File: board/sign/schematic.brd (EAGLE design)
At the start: 97.8 x 65.7 mm, 37 parts, among them IC1 STM32F207ZGT, IC3 LM3940, J1 DCJ0202, X2 22-23-2041

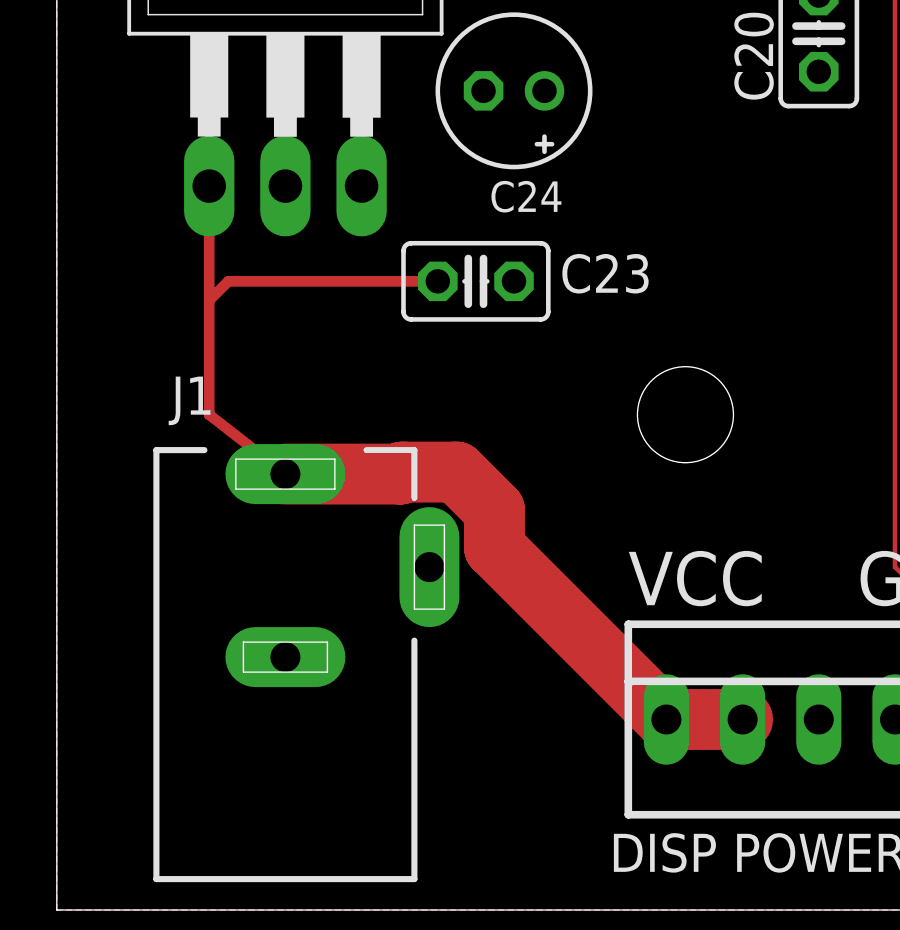
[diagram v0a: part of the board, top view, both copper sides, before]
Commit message: Board trace widths
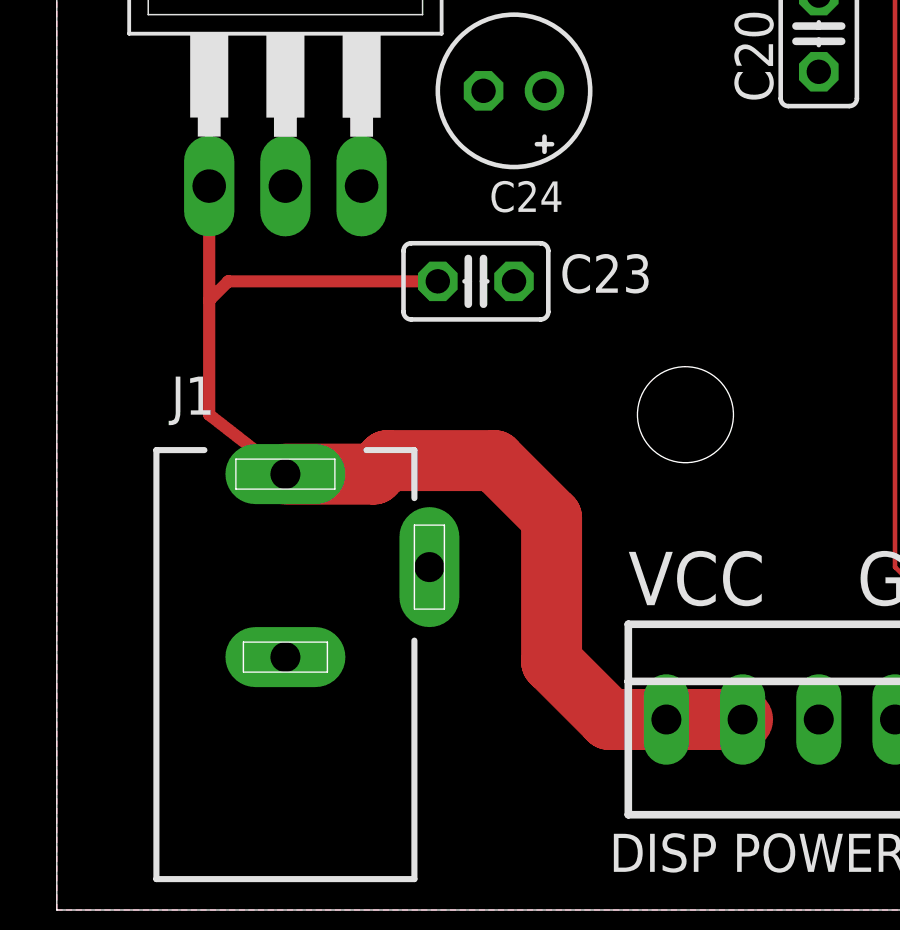
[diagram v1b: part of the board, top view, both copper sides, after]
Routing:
- net +5V: track 38.1 -> 40.5 mm
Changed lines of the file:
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@@
 <drawing>
 <settings>
-<setting alwaysvectorfont="no"/>
+<setting alwaysvectorfont="yes"/>
 <setting verticaltext="up"/>
 </settings>
@@
 <contactref element="IC3" pad="1"/>
 <contactref element="C23" pad="1"/>
-<wire x1="5.08" y1="24.13" x2="5.08" y2="20.32" width="0.3556" layer="1"/>
-<wire x1="5.08" y1="20.32" x2="5.08" y2="16.51" width="0.3556" layer="1"/>
-<wire x1="5.08" y1="16.51" x2="7.62" y2="14.53" width="0.3556" layer="1"/>
-<wire x1="11.52181875" y1="14.5984" x2="13.31818125" y2="14.5984" width="2.032" layer="1"/>
-<wire x1="13.31818125" y1="14.5984" x2="14.5884" y2="13.32818125" width="2.032" layer="1"/>
-<wire x1="14.5884" y1="13.32818125" x2="14.5884" y2="12.0816" width="2.032" layer="1"/>
-<wire x1="14.5884" y1="12.0816" x2="20.32" y2="6.35" width="2.032" layer="1"/>
-<wire x1="7.62" y1="14.53" x2="11.45341875" y2="14.53" width="2.032" layer="1"/>
-<wire x1="11.45341875" y1="14.53" x2="11.52181875" y2="14.5984" width="2.032" layer="1"/>
+<wire x1="5.08" y1="24.13" x2="5.08" y2="20.32" width="0.4064" layer="1"/>
+<wire x1="5.08" y1="20.32" x2="5.08" y2="16.51" width="0.4064" layer="1"/>
+<wire x1="5.08" y1="16.51" x2="7.62" y2="14.53" width="0.4064" layer="1"/>
+<wire x1="11.01381875" y1="14.9794" x2="14.58818125" y2="14.9794" width="2.032" layer="1"/>
+<wire x1="14.58818125" y1="14.9794" x2="16.4934" y2="13.07418125" width="2.032" layer="1"/>
+<wire x1="16.4934" y1="13.07418125" x2="16.4934" y2="8.2716" width="2.032" layer="1"/>
+<wire x1="18.415" y1="6.35" x2="20.32" y2="6.35" width="2.032" layer="1"/>
+<wire x1="18.415" y1="6.35" x2="16.4934" y2="8.2716" width="2.032" layer="1"/>
+<wire x1="7.62" y1="14.53" x2="10.56441875" y2="14.53" width="2.032" layer="1"/>
+<wire x1="10.56441875" y1="14.53" x2="11.01381875" y2="14.9794" width="2.032" layer="1"/>
 <wire x1="22.86" y1="6.35" x2="20.32" y2="6.35" width="2.032" layer="1"/>
-<wire x1="5.08" y1="20.32" x2="5.715" y2="20.955" width="0.3556" layer="1"/>
-<wire x1="5.715" y1="20.955" x2="12.7" y2="20.955" width="0.3556" layer="1"/>
+<wire x1="5.08" y1="20.32" x2="5.715" y2="20.955" width="0.4064" layer="1"/>
+<wire x1="5.715" y1="20.955" x2="12.7" y2="20.955" width="0.4064" layer="1"/>
 </signal>
 <signal name="DEBUG_TX">

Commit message: General trace cleanup
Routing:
- net RESET: track 104.9 -> 105.8 mm
- net B0: track 45.2 -> 45.8 mm
- net DEBUG_TX: track 37.4 -> 36.9 mm
- net D: track 36.0 -> 35.5 mm
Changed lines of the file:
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@@
 <contactref element="IC1" pad="115"/>
 <contactref element="JP1" pad="2"/>
-<wire x1="35.095" y1="42.58" x2="31.15" y2="42.58" width="0.1524" layer="1"/>
-<wire x1="31.15" y1="42.58" x2="28.448" y2="39.878" width="0.1524" layer="1"/>
-<wire x1="28.448" y1="39.878" x2="28.448" y2="14.732" width="0.1524" layer="1"/>
+<wire x1="35.095" y1="42.58" x2="30.642" y2="42.58" width="0.1524" layer="1"/>
+<wire x1="30.642" y1="42.58" x2="28.448" y2="40.386" width="0.1524" layer="1"/>
+<wire x1="28.448" y1="40.386" x2="28.448" y2="14.732" width="0.1524" layer="1"/>
 <wire x1="28.448" y1="14.732" x2="35.56" y2="7.62" width="0.1524" layer="1"/>
 </signal>
@@
 <contactref element="IC1" pad="116"/>
 <contactref element="JP1" pad="3"/>
-<wire x1="35.095" y1="42.08" x2="31.92" y2="42.08" width="0.1524" layer="1"/>
-<wire x1="31.92" y1="42.08" x2="28.956" y2="39.116" width="0.1524" layer="1"/>
+<wire x1="35.095" y1="42.08" x2="30.904" y2="42.08" width="0.1524" layer="1"/>
+<wire x1="30.904" y1="42.08" x2="28.956" y2="40.132" width="0.1524" layer="1"/>
 <wire x1="36.5506" y1="6.6294" x2="38.1" y2="5.08" width="0.1524" layer="1"/>
 <wire x1="36.5506" y1="8.030325" x2="36.5506" y2="6.6294" width="0.1524" layer="1"/>
-<wire x1="28.956" y1="39.116" x2="28.956" y2="15.624925" width="0.1524" layer="1"/>
+<wire x1="28.956" y1="40.132" x2="28.956" y2="15.624925" width="0.1524" layer="1"/>
 <wire x1="28.956" y1="15.624925" x2="36.5506" y2="8.030325" width="0.1524" layer="1"/>
 </signal>
@@
 <wire x1="35.1914" y1="33.4836" x2="35.095" y2="33.58" width="0.1524" layer="1"/>
 <wire x1="37.2686" y1="31.4064" x2="37.2686" y2="32.0796875" width="0.1524" layer="1"/>
-<wire x1="45.72" y1="10.16" x2="48.26" y2="7.62" width="0.1524" layer="16"/>
-<wire x1="46.340925" y1="23.30869375" x2="46.340925" y2="22.57221875" width="0.1524" layer="16"/>
+<wire x1="46.340925" y1="9.539075" x2="48.26" y2="7.62" width="0.1524" layer="16"/>
 <wire x1="45.72" y1="29.21" x2="45.72" y2="23.92961875" width="0.1524" layer="16"/>
-<wire x1="45.72" y1="21.95129375" x2="45.72" y2="10.16" width="0.1524" layer="16"/>
+<wire x1="46.340925" y1="23.30869375" x2="46.340925" y2="9.539075" width="0.1524" layer="16"/>
 <wire x1="45.72" y1="23.92961875" x2="46.340925" y2="23.30869375" width="0.1524" layer="16"/>
-<wire x1="46.340925" y1="22.57221875" x2="45.72" y2="21.95129375" width="0.1524" layer="16"/>
 </signal>
 <signal name="LAT">
@@
 <wire x1="48.26" y1="29.21" x2="48.26" y2="27.5932875" width="0.1524" layer="1"/>
 <wire x1="48.26" y1="27.5932875" x2="48.8736" y2="26.9796875" width="0.1524" layer="1"/>
-<wire x1="74.93" y1="39.37" x2="74.42" y2="39.37" width="0.1524" layer="1"/>
-<wire x1="74.42" y1="39.37" x2="71.12" y2="42.67" width="0.1524" layer="1"/>
+<wire x1="74.928" y1="40.894" x2="74.928" y2="39.372" width="0.1524" layer="1"/>
+<wire x1="74.93" y1="39.37" x2="74.928" y2="39.372" width="0.1524" layer="1"/>
+<wire x1="74.928" y1="40.894" x2="73.152" y2="42.67" width="0.1524" layer="1"/>
+<wire x1="73.152" y1="42.67" x2="71.12" y2="42.67" width="0.1524" layer="1"/>
 </signal>
 <signal name="TX">
@@
 <wire x1="56.485" y1="27.94" x2="56.345" y2="28.08" width="0.1524" layer="1"/>
 <wire x1="57.22723125" y1="27.94" x2="56.485" y2="27.94" width="0.1524" layer="1"/>
-<wire x1="95.25" y1="31.75" x2="88.4" y2="31.75" width="0.1524" layer="1"/>
-<wire x1="87.32" y1="30.67" x2="88.4" y2="31.75" width="0.1524" layer="1"/>
+<wire x1="95.25" y1="31.75" x2="94.742" y2="31.242" width="0.1524" layer="1"/>
+<wire x1="94.742" y1="31.242" x2="87.892" y2="31.242" width="0.1524" layer="1"/>
+<wire x1="87.32" y1="30.67" x2="87.892" y2="31.242" width="0.1524" layer="1"/>
 <wire x1="86.0914" y1="35.3646875" x2="86.2253125" y2="35.4986" width="0.1524" layer="1"/>
 <wire x1="87.32" y1="30.67" x2="87.32" y2="30.7467125" width="0.1524" layer="1"/>
@@
 <contactref element="IC2" pad="6"/>
 <wire x1="71.12" y1="32.67" x2="72.39" y2="31.4" width="0.1524" layer="1"/>
-<wire x1="72.5986" y1="17.4846875" x2="72.5986" y2="17.1614" width="0.1524" layer="1"/>
-<wire x1="72.5986" y1="17.1614" x2="73.17" y2="16.59" width="0.1524" layer="1"/>
-<wire x1="72.39" y1="17.6932875" x2="72.5986" y2="17.4846875" width="0.1524" layer="1"/>
+<wire x1="73.17" y1="16.9132875" x2="73.17" y2="16.59" width="0.1524" layer="1"/>
+<wire x1="73.17" y1="16.9132875" x2="72.39" y2="17.6932875" width="0.1524" layer="1"/>
 <wire x1="72.39" y1="31.4" x2="72.39" y2="17.6932875" width="0.1524" layer="1"/>
 </signal>
@@
 <contactref element="JP2" pad="5"/>
 <wire x1="92.71" y1="33.02" x2="95.25" y2="35.56" width="0.1524" layer="1"/>
-<wire x1="95.25" y1="35.56" x2="95.25" y2="52.07" width="0.1524" layer="1"/>
-<wire x1="95.25" y1="52.07" x2="91.44" y2="55.88" width="0.1524" layer="1"/>
-<wire x1="91.44" y1="55.88" x2="85.09" y2="55.88" width="0.1524" layer="1"/>
+<wire x1="95.25" y1="35.56" x2="95.25" y2="51.181" width="0.1524" layer="1"/>
+<wire x1="95.25" y1="51.181" x2="90.551" y2="55.88" width="0.1524" layer="1"/>
+<wire x1="90.551" y1="55.88" x2="85.09" y2="55.88" width="0.1524" layer="1"/>
 </signal>
 <signal name="N$4">
@@
 <wire x1="89.025" y1="42.67" x2="90.17" y2="43.815" width="0.1524" layer="1"/>
 <wire x1="90.17" y1="50.165" x2="88.9" y2="51.435" width="0.1524" layer="1"/>
-<wire x1="88.9" y1="51.435" x2="83.185" y2="51.435" width="0.1524" layer="1"/>
-<wire x1="83.185" y1="51.435" x2="77.47" y2="55.88" width="0.1524" layer="1"/>
+<wire x1="88.9" y1="51.435" x2="81.915" y2="51.435" width="0.1524" layer="1"/>
+<wire x1="81.915" y1="51.435" x2="77.47" y2="55.88" width="0.1524" layer="1"/>
 <wire x1="90.17" y1="43.815" x2="90.17" y2="50.165" width="0.1524" layer="1"/>
 </signal>
@@
 <contactref element="JP2" pad="3"/>
 <wire x1="87.32" y1="40.67" x2="91.41" y2="40.67" width="0.1524" layer="1"/>
-<wire x1="91.41" y1="40.67" x2="91.44" y2="40.64" width="0.1524" layer="1"/>
-<wire x1="91.44" y1="40.64" x2="92.71" y2="41.91" width="0.1524" layer="1"/>
-<wire x1="92.71" y1="41.91" x2="92.71" y2="50.8" width="0.1524" layer="1"/>
+<wire x1="92.71" y1="50.8" x2="92.71" y2="41.91" width="0.1524" layer="1"/>
 <wire x1="91.1352" y1="52.3748" x2="83.82" y2="52.3748" width="0.1524" layer="1"/>
 <wire x1="92.71" y1="50.8" x2="91.1352" y2="52.3748" width="0.1524" layer="1"/>
 <wire x1="83.82" y1="52.3748" x2="81.28" y2="54.9148" width="0.1524" layer="1"/>
 <wire x1="81.28" y1="54.9148" x2="80.01" y2="55.88" width="0.1524" layer="1"/>
+<wire x1="92.71" y1="41.91" x2="91.47" y2="40.67" width="0.1524" layer="1"/>
+<wire x1="91.47" y1="40.67" x2="91.41" y2="40.67" width="0.1524" layer="1"/>
 </signal>
 <signal name="SWDIO">
 <contactref element="JP3" pad="4"/>
 <contactref element="IC1" pad="105"/>
-<wire x1="38.4498" y1="46.65375" x2="38.27125" y2="46.4752" width="0.3048" layer="1"/>
-<wire x1="38.27125" y1="46.4752" x2="36.66875" y2="46.4752" width="0.3048" layer="1"/>
+<wire x1="38.4498" y1="46.65375" x2="38.27125" y2="46.4752" width="0.1524" layer="1"/>
+<wire x1="38.27125" y1="46.4752" x2="36.66875" y2="46.4752" width="0.1524" layer="1"/>
 <wire x1="38.47" y1="47.455" x2="38.4498" y2="47.4348" width="0.3048" layer="1"/>
-<wire x1="38.4498" y1="47.4348" x2="38.4498" y2="46.65375" width="0.3048" layer="1"/>
-<wire x1="36.66875" y1="46.4752" x2="36.15395" y2="46.99" width="0.3048" layer="1"/>
-<wire x1="36.15395" y1="46.99" x2="21.59" y2="46.99" width="0.3048" layer="1"/>
+<wire x1="38.4498" y1="47.4348" x2="38.4498" y2="46.65375" width="0.1524" layer="1"/>
+<wire x1="36.66875" y1="46.4752" x2="36.15395" y2="46.99" width="0.1524" layer="1"/>
+<wire x1="36.15395" y1="46.99" x2="21.59" y2="46.99" width="0.1524" layer="1"/>
 </signal>
 <signal name="SWCLK">
